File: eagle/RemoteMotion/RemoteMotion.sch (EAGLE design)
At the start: 7 parts, among them J1 1

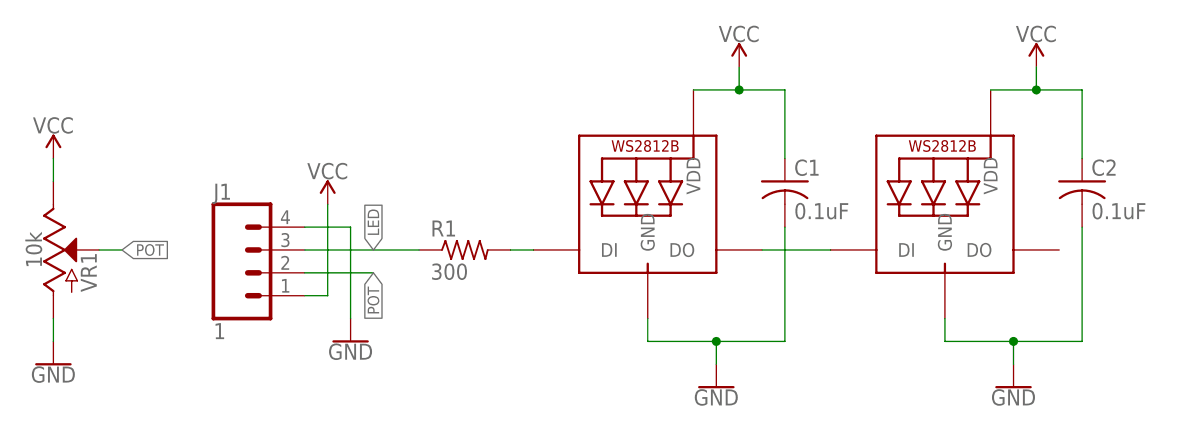
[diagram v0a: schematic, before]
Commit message: Move to managed libarary for 3d parts
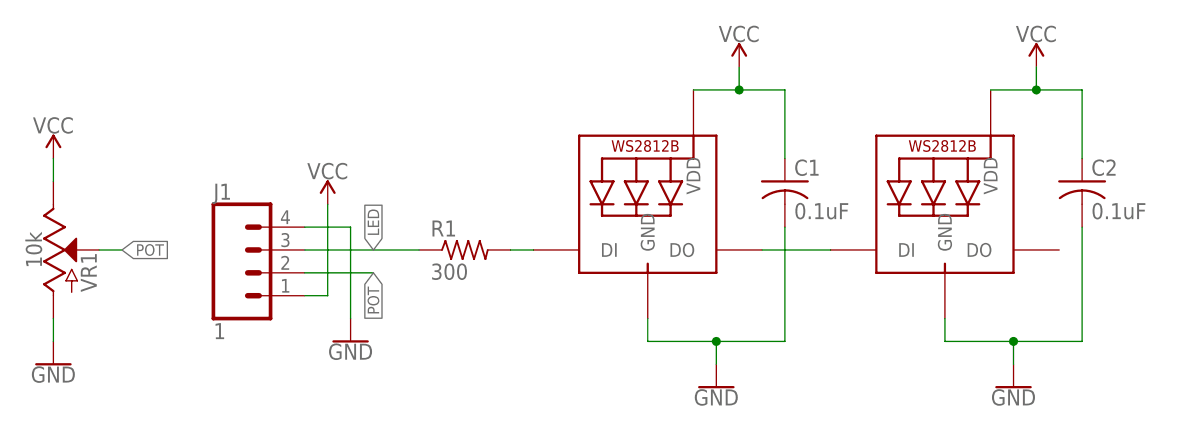
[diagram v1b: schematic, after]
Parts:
- C1, C2: device rcl:C-USC0805 -> RemoteMotion:C-USC0805
- J1: device SparkFun-Connectors:CONN_04JST-PTH -> RemoteMotion:CONN_04JST-PTH
- LED1, LED2: device adafruit:WS2812B5050 -> RemoteMotion:WS2812B5050
- R1: device rcl:R-US_R0805 -> RemoteMotion:R-US_R0805
- VR1: device SparkFun-Resistors:POTENTIOMETER_SLIDE-60MM-1/2W-20% -> RemoteMotion:POTENTIOMETER_SLIDE-60MM-1/2W-20%
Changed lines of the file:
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@@
 <?xml version="1.0" encoding="utf-8"?>
 <!DOCTYPE eagle SYSTEM "eagle.dtd">
-<eagle version="8.7.1">
+<eagle version="9.0.0">
 <drawing>
 <settings>
@@
 </classes>
 <parts>
-<part name="VR1" library="SparkFun-Resistors" deviceset="POTENTIOMETER_SLIDE" device="-60MM-1/2W-20%" value="10k"/>
-<part name="J1" library="SparkFun-Connectors" deviceset="CONN_04" device="JST-PTH" value="1"/>
-<part name="LED1" library="adafruit" deviceset="WS2812B" device="5050"/>
-<part name="GND1" library="SparkFun-PowerSymbols" deviceset="GND" device=""/>
-<part name="SUPPLY1" library="SparkFun-PowerSymbols" deviceset="VCC" device=""/>
-<part name="SUPPLY2" library="SparkFun-PowerSymbols" deviceset="VCC" device=""/>
-<part name="GND2" library="SparkFun-PowerSymbols" deviceset="GND" device=""/>
-<part name="R1" library="rcl" library_urn="urn:adsk.eagle:library:334" deviceset="R-US_" device="R0805" package3d_urn="urn:adsk.eagle:package:23553/2" value="300"/>
-<part name="C1" library="rcl" library_urn="urn:adsk.eagle:library:334" deviceset="C-US" device="C0805" package3d_urn="urn:adsk.eagle:package:23617/2" value="0.1uF"/>
-<part name="SUPPLY3" library="SparkFun-PowerSymbols" deviceset="VCC" device=""/>
-<part name="GND3" library="SparkFun-PowerSymbols" deviceset="GND" device=""/>
-<part name="LED2" library="adafruit" deviceset="WS2812B" device="5050"/>
-<part name="C2" library="rcl" library_urn="urn:adsk.eagle:library:334" deviceset="C-US" device="C0805" package3d_urn="urn:adsk.eagle:package:23617/2" value="0.1uF"/>
-<part name="SUPPLY4" library="SparkFun-PowerSymbols" deviceset="VCC" device=""/>
-<part name="GND4" library="SparkFun-PowerSymbols" deviceset="GND" device=""/>
+<part name="VR1" library="RemoteMotion" library_urn="urn:adsk.eagle:library:2810894" deviceset="POTENTIOMETER_SLIDE" device="-60MM-1/2W-20%" package3d_urn="urn:adsk.eagle:package:2811214/2" value="10k"/>
+<part name="J1" library="RemoteMotion" library_urn="urn:adsk.eagle:library:2810894" deviceset="CONN_04" device="JST-PTH" package3d_urn="urn:adsk.eagle:package:2811204/1" value="1"/>
+<part name="LED1" library="RemoteMotion" library_urn="urn:adsk.eagle:library:2810894" deviceset="WS2812B" device="5050" package3d_urn="urn:adsk.eagle:package:2811216/1"/>
+<part name="GND1" library="RemoteMotion" library_urn="urn:adsk.eagle:library:2810894" deviceset="GND" device=""/>
+<part name="SUPPLY1" library="RemoteMotion" library_urn="urn:adsk.eagle:library:2810894" deviceset="VCC" device=""/>
+<part name="SUPPLY2" library="RemoteMotion" library_urn="urn:adsk.eagle:library:2810894" deviceset="VCC" device=""/>
+<part name="GND2" library="RemoteMotion" library_urn="urn:adsk.eagle:library:2810894" deviceset="GND" device=""/>
+<part name="R1" library="RemoteMotion" library_urn="urn:adsk.eagle:library:2810894" deviceset="R-US_" device="R0805" package3d_urn="urn:adsk.eagle:package:2811399/2" value="300"/>
+<part name="C1" library="RemoteMotion" library_urn="urn:adsk.eagle:library:2810894" deviceset="C-US" device="C0805" package3d_urn="urn:adsk.eagle:package:2811338/2" value="0.1uF"/>
+<part name="SUPPLY3" library="RemoteMotion" library_urn="urn:adsk.eagle:library:2810894" deviceset="VCC" device=""/>
+<part name="GND3" library="RemoteMotion" library_urn="urn:adsk.eagle:library:2810894" deviceset="GND" device=""/>
+<part name="LED2" library="RemoteMotion" library_urn="urn:adsk.eagle:library:2810894" deviceset="WS2812B" device="5050" package3d_urn="urn:adsk.eagle:package:2811216/1"/>
+<part name="C2" library="RemoteMotion" library_urn="urn:adsk.eagle:library:2810894" deviceset="C-US" device="C0805" package3d_urn="urn:adsk.eagle:package:2811338/2" value="0.1uF"/>
+<part name="SUPPLY4" library="RemoteMotion" library_urn="urn:adsk.eagle:library:2810894" deviceset="VCC" device=""/>
+<part name="GND4" library="RemoteMotion" library_urn="urn:adsk.eagle:library:2810894" deviceset="GND" device=""/>
 </parts>
 <sheets>
@@
 packages will not be understood (or retained) with this version.
 </note>
-<note version="8.4" severity="warning">
-Since Version 8.4, EAGLE supports properties for SPICE simulation.
-Probes in schematics and SPICE mapping objects found in parts and library devices
-will not be understood with this version. Update EAGLE to the latest version
-for full support of SPICE simulation.
-</note>
 </compatibility>
